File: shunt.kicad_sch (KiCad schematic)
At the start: 38 parts, among them J2 Screw_Terminal_01x03, U2 INA219AxD

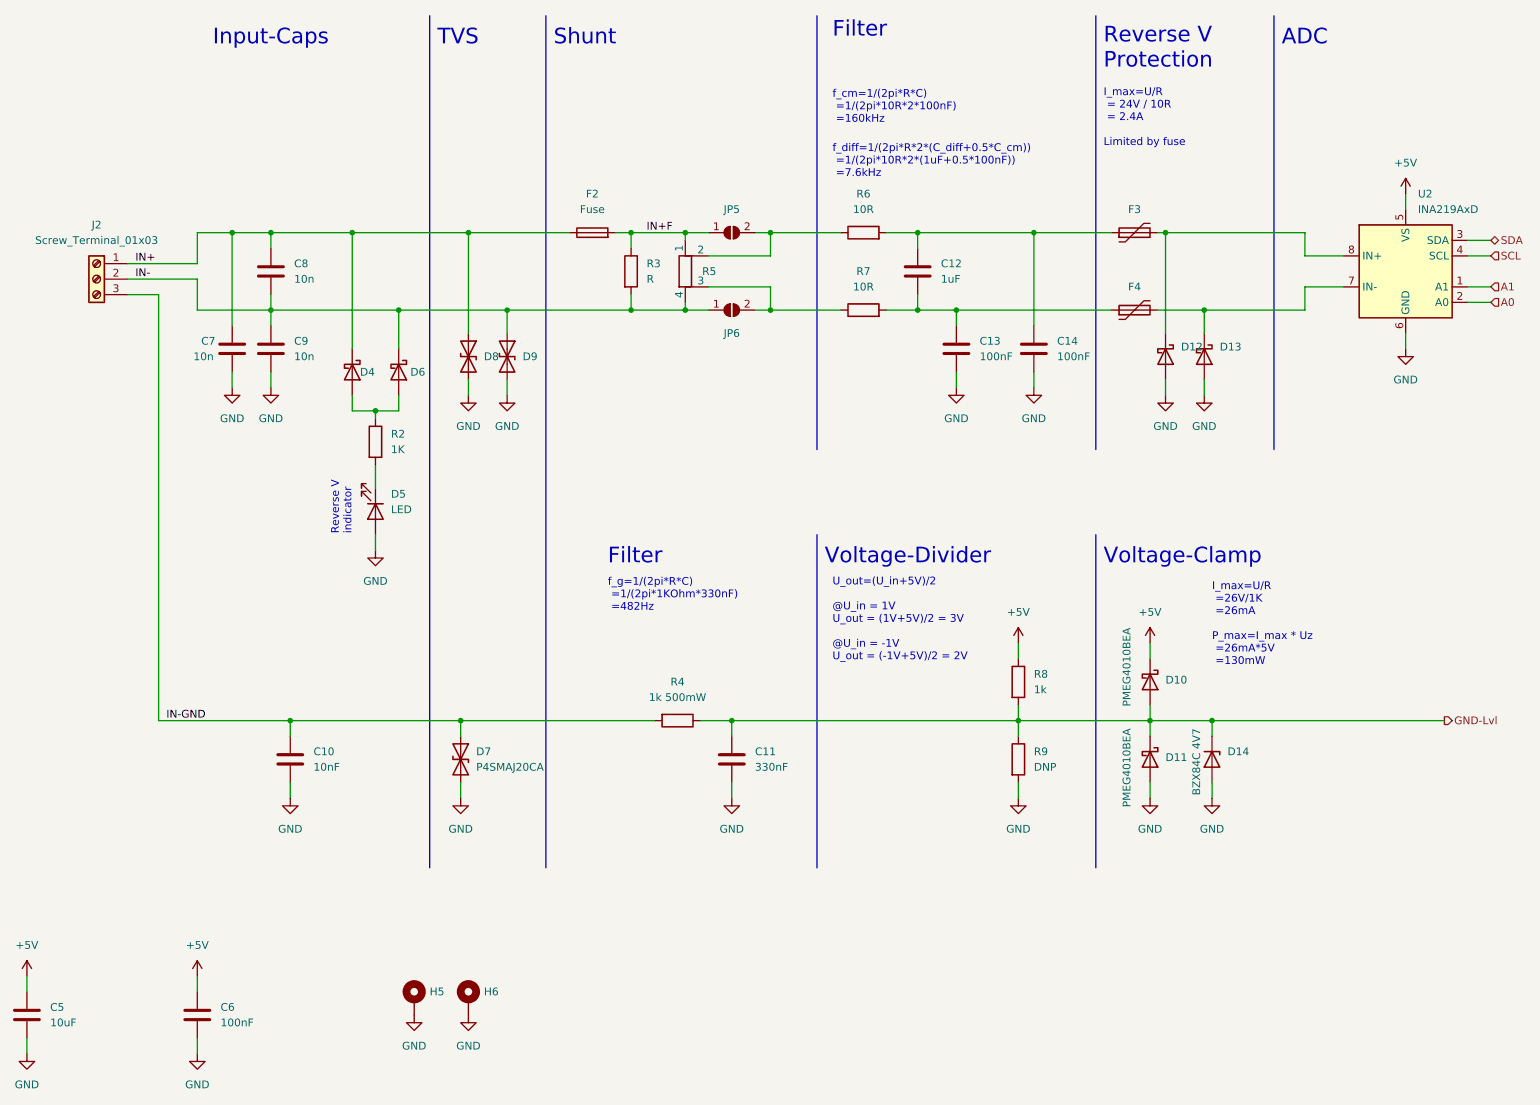
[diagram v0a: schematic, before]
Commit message: Add a lot of nice to haves
* Jumpers to bridge isolation
* I2C pullups with jumpers for input
* Labels on input connectors
* Geographic reference counts
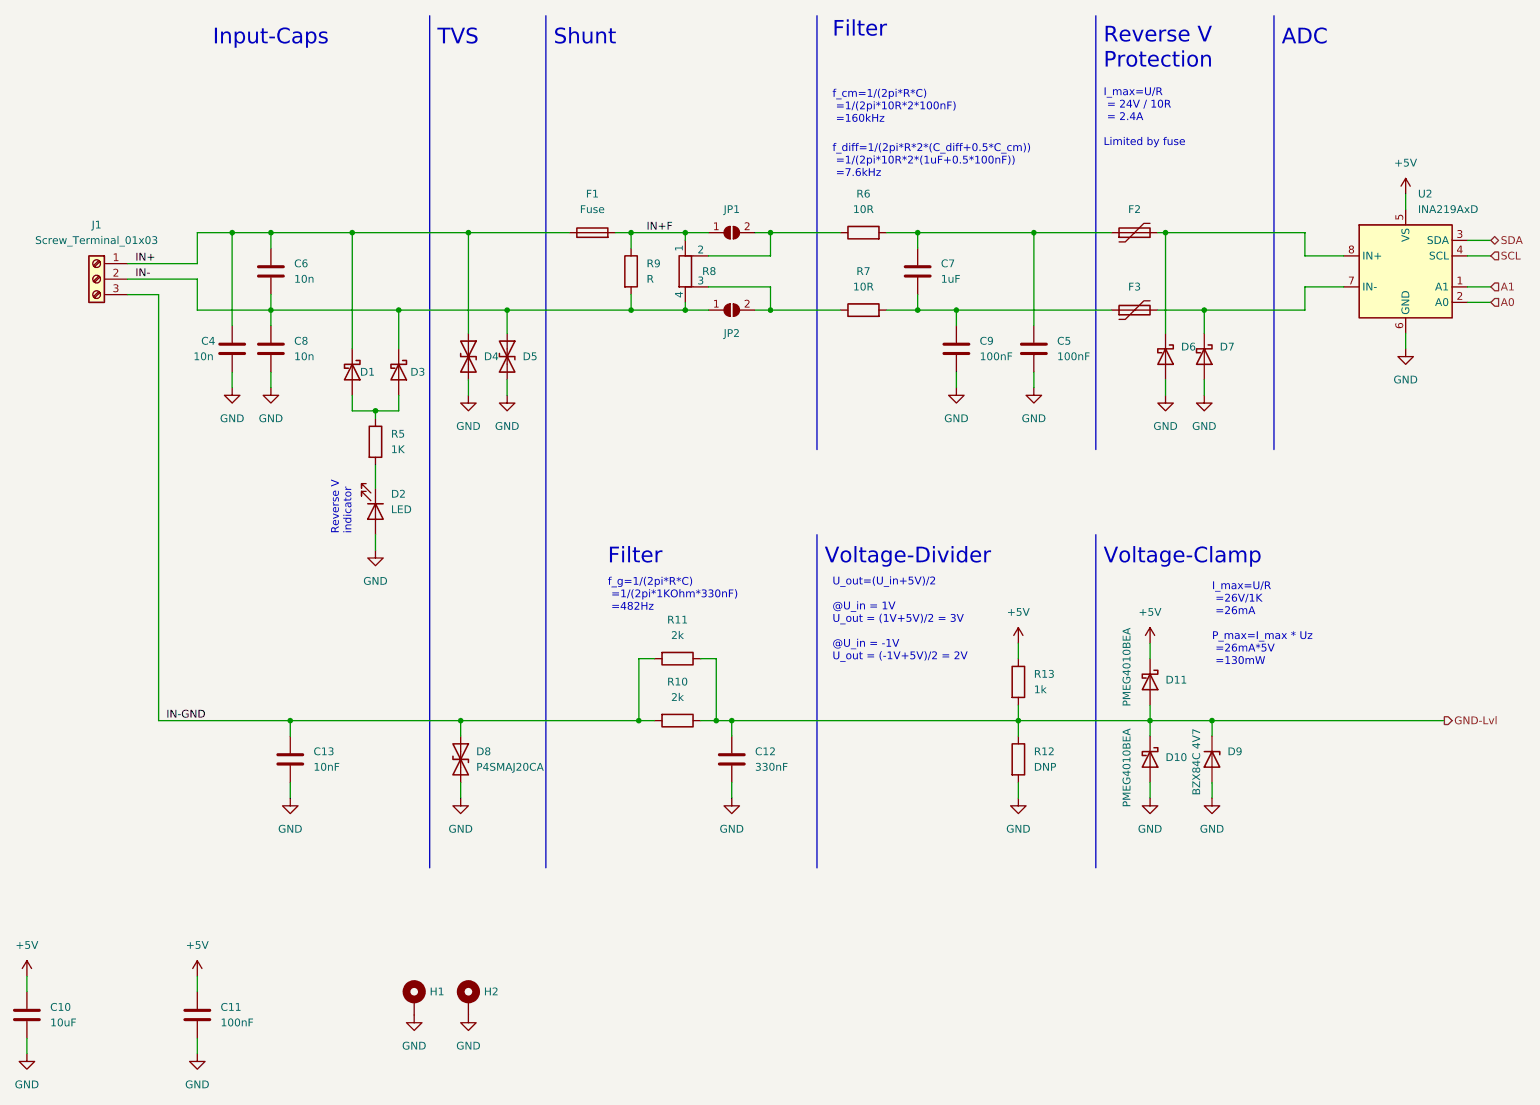
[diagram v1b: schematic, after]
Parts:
- added R11: 2k, Resistor_SMD:R_1206_3216Metric_Pad1.30x1.75mm_HandSolder, symbol Device:R
- R10: renamed from R4; value 1k 500mW -> 2k
- R12: renamed from R9; now left out of the parts list
- renumbered C5 to C10, C6 to C11, C11 to C12, C10 to C13, C7 to C4, C14 to C5, C8 to C6, C12 to C7, C9 to C8, C13 to C9, D4 to D1, D11 to D10, D10 to D11, D5 to D2, D6 to D3, D8 to D4, D9 to D5, D12 to D6, D13 to D7, D7 to D8, D14 to D9, F2 to F1, F3 to F2, F4 to F3, H5 to H1, H6 to H2, J2 to J1, JP5 to JP1, JP6 to JP2, R8 to R13, R2 to R5, R5 to R8, R3 to R9
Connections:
- net GND-Lvl: now also R11.1
- net IN-GND: now also R11.2

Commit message: Cleanup custom footprints and symbols
This makes the names more descriptive and gets rid of unused
symbols.
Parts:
- F1: footprint R-Manganin:IMaxx H7810 -> Project_Footprints:iMaXX-H7810
- J1: footprint R-Manganin:My-2604-1103 -> Project_Footprints:Wago_2604-1103
- R8: footprint R-Manganin:SIP -> Project_Footprints:R_Shunt_Isabellenhuette_PBV
- R9: footprint R-Manganin:Dual-2512-1206-Handsolder -> Project_Footprints:R_Dual_2512_1206_Handsolder
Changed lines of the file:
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@@
       (effects (font (size 1.27 1.27)) (justify left))
     )
-    (property "Footprint" "R-Manganin:Dual-2512-1206-Handsolder" (id 2) (at 120.142 57.15 90)
+    (property "Footprint" "Project_Footprints:R_Dual_2512_1206_Handsolder" (id 2) (at 120.142 57.15 90)
       (effects (font (size 1.27 1.27)) hide)
     )
@@
       (effects (font (size 1.27 1.27)) (justify right) hide)
     )
-    (property "Footprint" "R-Manganin:SIP" (id 2) (at 129.032 57.15 90)
+    (property "Footprint" "Project_Footprints:R_Shunt_Isabellenhuette_PBV" (id 2) (at 129.032 57.15 90)
       (effects (font (size 1.27 1.27)) hide)
     )
@@
     (property "Reference" "F1" (id 0) (at 115.57 44.45 90))
     (property "Value" "Fuse" (id 1) (at 115.57 46.99 90))
-    (property "Footprint" "R-Manganin:IMaxx H7810" (id 2) (at 115.57 52.578 90)
+    (property "Footprint" "Project_Footprints:iMaXX-H7810" (id 2) (at 115.57 52.578 90)
       (effects (font (size 1.27 1.27)) hide)
     )
@@
     (property "Reference" "J1" (id 0) (at 34.29 49.53 0))
     (property "Value" "Screw_Terminal_01x03" (id 1) (at 34.29 52.07 0))
-    (property "Footprint" "R-Manganin:My-2604-1103" (id 2) (at 34.29 58.42 0)
-      (effects (font (size 1.27 1.27)) hide)
-    )
+    (property "Footprint" "Project_Footprints:Wago_2604-1103" (id 2) (at 34.29 58.42 0)
+      (effects (font (size 1.27 1.27)) hide)
+    )

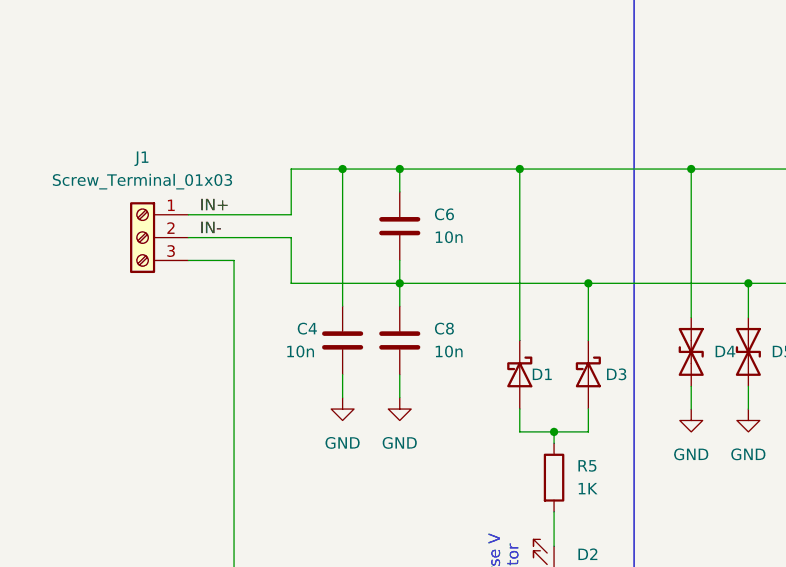
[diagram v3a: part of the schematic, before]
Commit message: Add LCSC order numbers to more easily order at JLCPCB
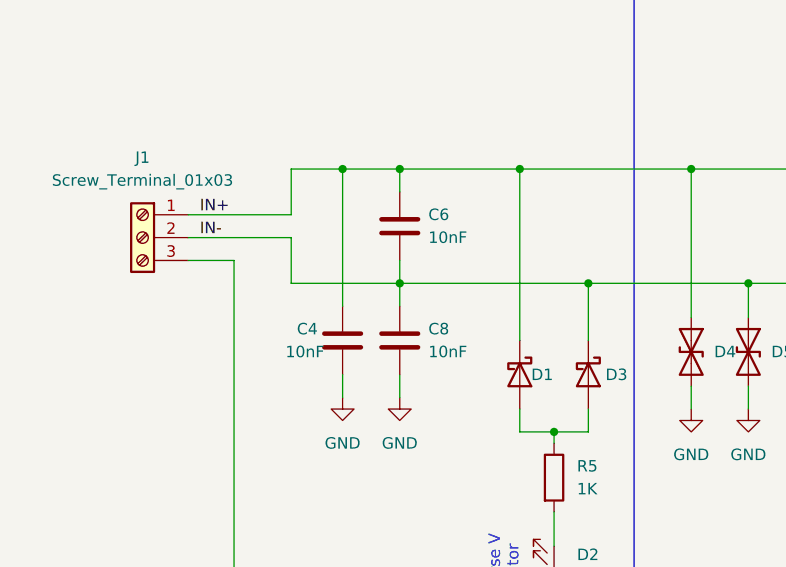
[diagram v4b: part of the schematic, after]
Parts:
- C10: LCSC Part # (none) -> C13585
- C11, C5, C9: LCSC Part # (none) -> C14663
- C12: LCSC Part # (none) -> C274377
- C13: LCSC Part # (none) -> C57112
- C4, C6, C8: value 10n -> 10nF; LCSC Part # (none) -> C57112
- C7: LCSC Part # (none) -> C1848
- D1, D10, D11, D3, D6, D7: LCSC Part # (none) -> C36975
- D2: LCSC Part # (none) -> C2286
- D4, D5: value P4SMAJ26CA -> P4SMAJ20CA; LCSC Part # (none) -> C391567
- D8: LCSC Part # (none) -> C391567
- D9: LCSC Part # (none) -> C118567
- F2, F3: value Fuse_Small -> 1206L016WR; LCSC Part # (none) -> C151161
- H1, H2, R8, R9: now left out of the parts list
- R10, R11: LCSC Part # (none) -> C17944
- R13: LCSC Part # (none) -> C4410
- R5: LCSC Part # (none) -> C21190
- R6, R7: LCSC Part # (none) -> C17903
- U2: LCSC Part # (none) -> C138706

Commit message: Remove PCB only parts from BOM
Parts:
- JP1, JP2: now left out of the parts list
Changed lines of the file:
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@@
   )
   (symbol (lib_id "Jumper:SolderJumper_2_Open") (at 138.43 50.8 0) (unit 1)
-    (in_bom yes) (on_board yes) (fields_autoplaced)
+    (in_bom no) (on_board yes) (fields_autoplaced)
     (property "Reference" "JP1" (id 0) (at 138.43 46.99 0))
     (property "Value" "SolderJumper_2_Open" (id 1) (at 138.43 46.99 0)
@@
   )
   (symbol (lib_id "Jumper:SolderJumper_2_Open") (at 138.43 63.5 0) (unit 1)
-    (in_bom yes) (on_board yes)
+    (in_bom no) (on_board yes)
     (property "Reference" "JP2" (id 0) (at 138.43 67.31 0))
     (property "Value" "SolderJumper_2_Open" (id 1) (at 138.43 59.69 0)

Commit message: Add JLCPCB rotation offsets
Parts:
- D9: JLCPCB Rotation Offset (none) -> 180
- U2: JLCPCB Rotation Offset (none) -> -90
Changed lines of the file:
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@@
+      (effects (font (size 1.27 1.27)) hide)
+    )
+    (property "JLCPCB Rotation Offset" "180" (id 5) (at 217.17 137.16 0)
       (effects (font (size 1.27 1.27)) hide)
     )
@@
       (effects (font (size 1.27 1.27)) hide)
     )
+    (property "JLCPCB Rotation Offset" "-90" (id 5) (at 248.92 57.15 0)
+      (effects (font (size 1.27 1.27)) hide)
+    )

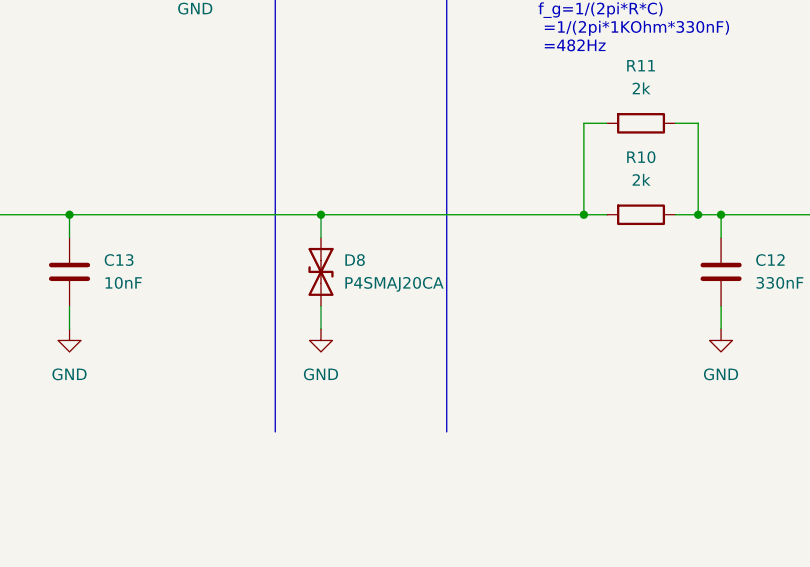
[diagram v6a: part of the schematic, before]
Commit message: Add labels to board and update not available component
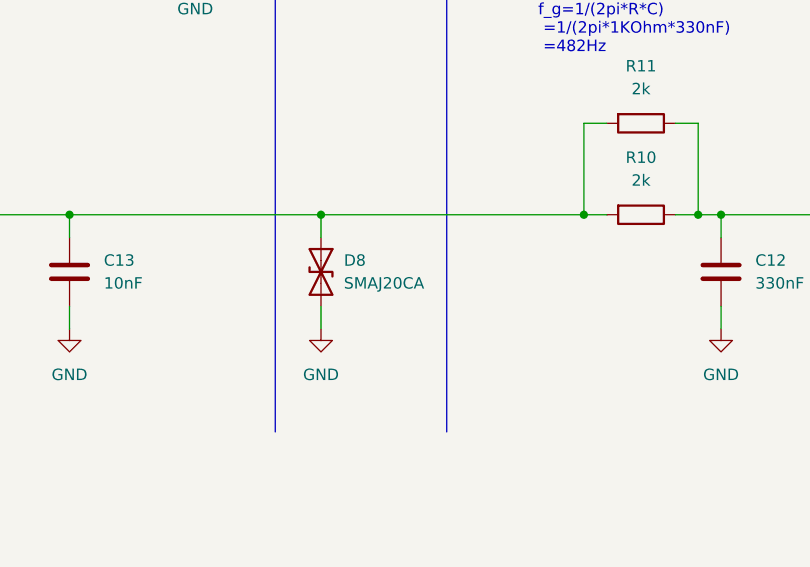
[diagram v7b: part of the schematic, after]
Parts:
- D4, D5, D8: value P4SMAJ20CA -> SMAJ20CA; LCSC Part # C391567 -> C309871
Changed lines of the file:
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@@
       (effects (font (size 1.27 1.27)) (justify left))
     )
-    (property "Value" "P4SMAJ20CA" (id 1) (at 96.52 138.4299 90)
+    (property "Value" "SMAJ20CA" (id 1) (at 96.52 138.4299 90)
       (effects (font (size 1.27 1.27)) (justify left))
     )
@@
       (effects (font (size 1.27 1.27)) hide)
     )
-    (property "LCSC Part #" "C391567" (id 4) (at 93.98 137.16 0)
+    (property "LCSC Part #" "C309871" (id 4) (at 93.98 137.16 0)
       (effects (font (size 1.27 1.27)) hide)
     )
@@
       (effects (font (size 1.27 1.27)) (justify left))
     )
-    (property "Value" "P4SMAJ20CA" (id 1) (at 97.79 72.3899 90)
+    (property "Value" "SMAJ20CA" (id 1) (at 97.79 72.3899 90)
       (effects (font (size 1.27 1.27)) (justify left) hide)
     )
@@
       (effects (font (size 1.27 1.27)) hide)
     )
-    (property "LCSC Part #" "C391567" (id 4) (at 95.25 71.12 0)
+    (property "LCSC Part #" "C309871" (id 4) (at 95.25 71.12 0)
       (effects (font (size 1.27 1.27)) hide)
     )
@@
       (effects (font (size 1.27 1.27)) (justify left))
     )
-    (property "Value" "P4SMAJ20CA" (id 1) (at 104.14 72.3899 90)
+    (property "Value" "SMAJ20CA" (id 1) (at 104.14 72.3899 90)
       (effects (font (size 1.27 1.27)) (justify left) hide)
     )
@@
       (effects (font (size 1.27 1.27)) hide)
     )
-    (property "LCSC Part #" "C391567" (id 4) (at 101.6 71.12 0)
-      (effects (font (size 1.27 1.27)) hide)
-    )
+    (property "LCSC Part #" "C309871" (id 4) (at 101.6 71.12 0)
+      (effects (font (size 1.27 1.27)) hide)
+    )
